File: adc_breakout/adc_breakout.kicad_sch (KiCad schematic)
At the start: 26 parts, among them IC101 PCM1863DBT, J101 Conn_Coaxial_x2, J102 Conn_01x02, J103 Conn_02x06_Odd_Even, U101 AZ1117-3.3, Y101 Crystal

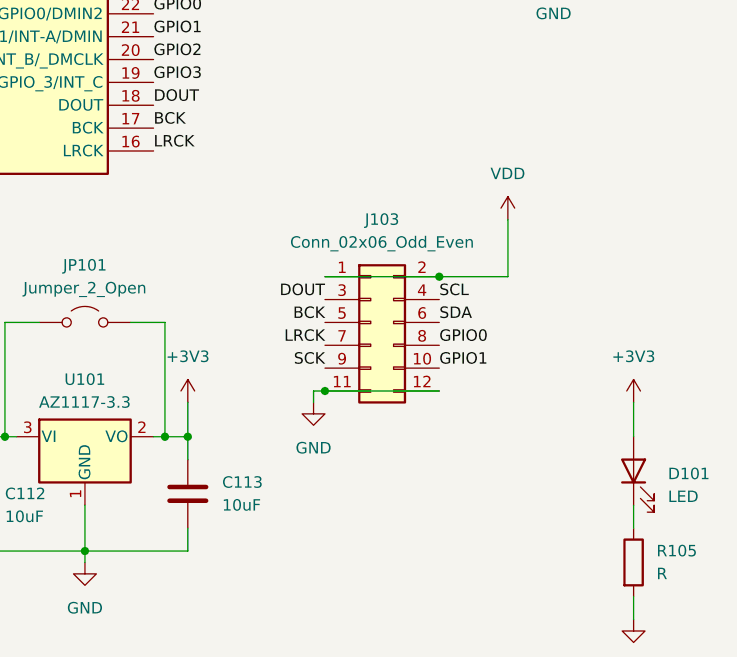
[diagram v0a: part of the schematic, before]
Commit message: Made breakboard compatible
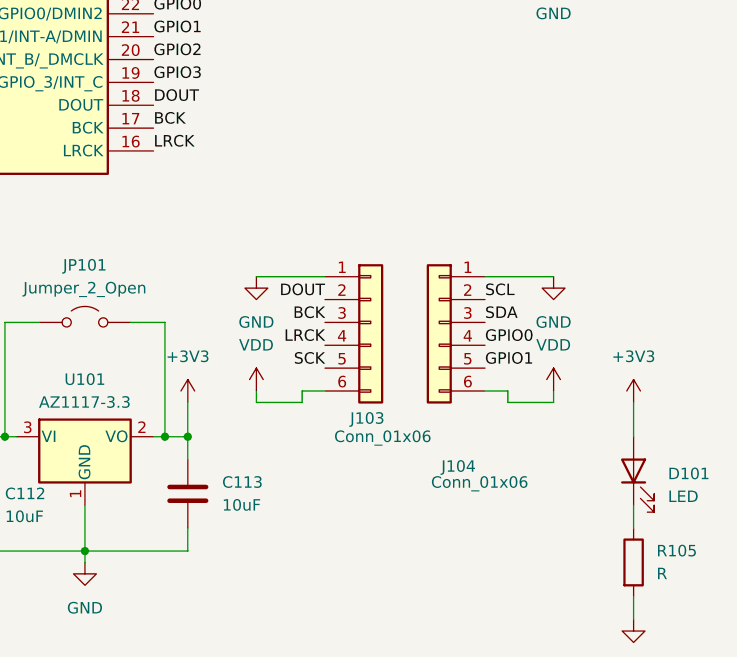
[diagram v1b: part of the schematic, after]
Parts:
- removed J103: Conn_02x06_Odd_Even, Connector_PinHeader_2.54mm:PinHeader_2x06_P2.54mm_Vertical, symbol Connector_Generic:Conn_02x06_Odd_Even
- added J103, J104: Conn_01x06, Connector_PinHeader_2.54mm:PinHeader_1x06_P2.54mm_Vertical, symbol Connector_Generic:Conn_01x06
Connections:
- net BCK: now also J103.3 (Pin_3)
- net DOUT: now also J103.2 (Pin_2)
- net GND: now also J103.1 (Pin_1), J104.1 (Pin_1)
- net GPIO0: now also J104.4 (Pin_4)
- net GPIO1: now also J104.5 (Pin_5)
- net LRCK: now also J103.4 (Pin_4)
- net SCK: now also J103.5 (Pin_5)
- net SCL: now also J104.2 (Pin_2)
- net SDA: now also J104.3 (Pin_3)
- net VDD: now also J103.6 (Pin_6), J104.6 (Pin_6)
